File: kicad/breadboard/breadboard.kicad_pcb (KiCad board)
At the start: 2 copper layers, 100 x 100 mm, 22 parts, among them J1 Conn_01x08, J3 Conn_01x08, J4 Conn_01x30, J49 Barrel_Jack, J5 Conn_01x30, J6 Conn_01x30, J7 Conn_01x30, U1 AMS1117-3V3, U2 L7805, U4 bboard_3rows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

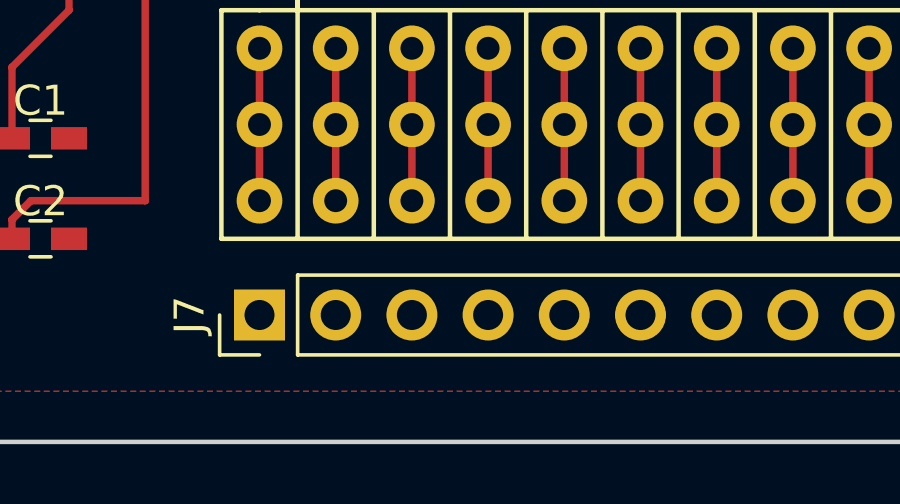
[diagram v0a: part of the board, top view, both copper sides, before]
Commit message: Revert "Add gitignore"
This reverts commit 1d0808174f2c1fbc4e2cf73c68065f4eadfb9096.
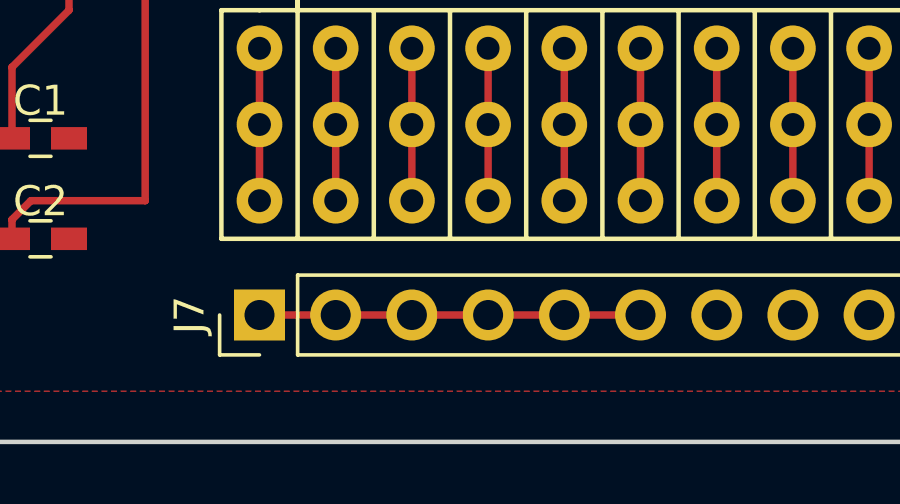
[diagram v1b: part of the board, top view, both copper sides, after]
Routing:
- net GND: track 59.8 -> 72.5 mm

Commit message: Add gitignore
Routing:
- net GND: track 72.5 -> 59.8 mm
